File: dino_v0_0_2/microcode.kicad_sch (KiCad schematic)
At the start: 8 parts, among them U15 AT28C64B, U16 74LS244N, U17 74LS244N, U9 AT28C64B

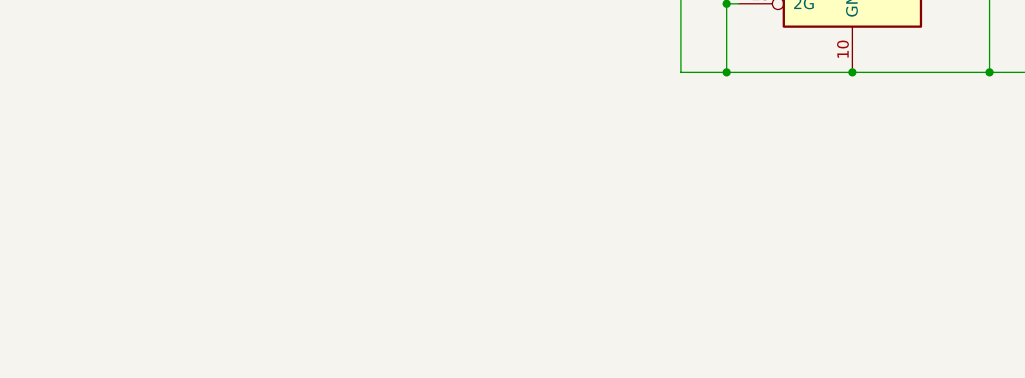
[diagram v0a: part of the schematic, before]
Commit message: feat(dino): generate + stamp per-sheet I/O contracts
Each module's boundary signals (IN/OUT/BIDIR with counterpart sheets)
derived from the kicad-cli netlist and placed as a text block on the
physical sheet, so a bench rig knows exactly what to drive and observe
per board. kicad_contracts.py regenerates both the markdown and the
stamps idempotently; stamping verified electrically neutral.
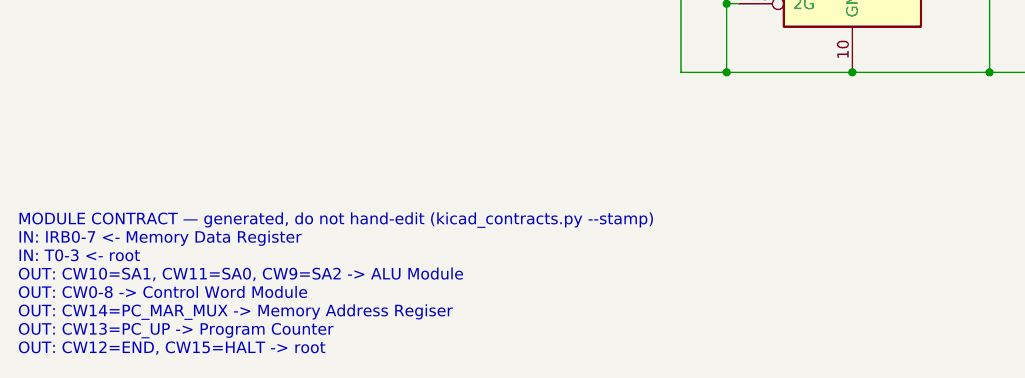
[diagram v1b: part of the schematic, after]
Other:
- note added: "MODULE CONTRACT — generated, do not hand-edit (kicad_contracts.py --stamp) IN: IRB0-7 <- Memory Data Register IN: T0-3 <- root OUT: CW10=SA1, CW11=SA0, CW9=SA2 -> ALU Module OUT: CW0-8 -> Control Word Module OUT: CW14=PC_MAR_MUX -> Memory Address Regiser OUT: CW13=PC_UP -> Program Counter OUT: CW12=END, CW15=HALT -> root"
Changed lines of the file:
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@@
+		)
+	)
+	(text "MODULE CONTRACT — generated, do not hand-edit (kicad_contracts.py --stamp)\nIN: IRB0-7 <- Memory Data Register\nIN: T0-3 <- root\nOUT: CW10=SA1, CW11=SA0, CW9=SA2 -> ALU Module\nOUT: CW0-8 -> Control Word Module\nOUT: CW14=PC_MAR_MUX -> Memory Address Regiser\nOUT: CW13=PC_UP -> Program Counter\nOUT: CW12=END, CW15=HALT -> root"
+		(exclude_from_sim no)
+		(at 15.24 171.29 0)
+		(effects
+			(font
+				(size 1.27 1.27)
+			)
+			(justify left bottom)
 		)
 	)
